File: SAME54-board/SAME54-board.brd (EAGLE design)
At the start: 70.8 x 119.4 mm, 33 parts, among them IC1 ATSAME54N20A-AUT, J1 GSD09002SEU, J2 CON-SOCJ-2155

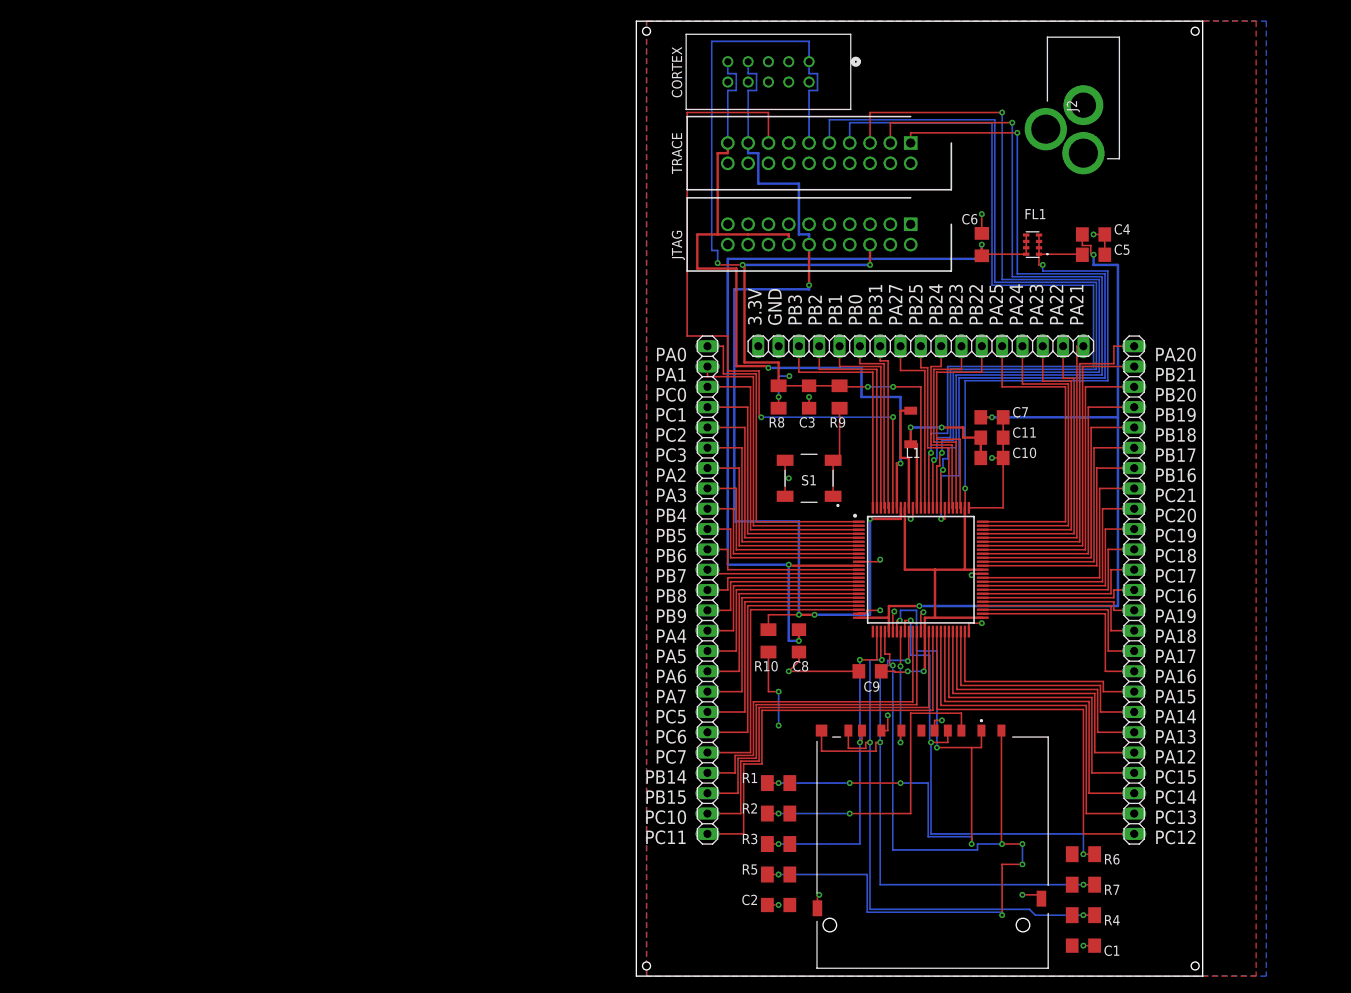
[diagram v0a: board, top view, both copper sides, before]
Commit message: Removed molex adapters and recplaed with single pin hole for each signal
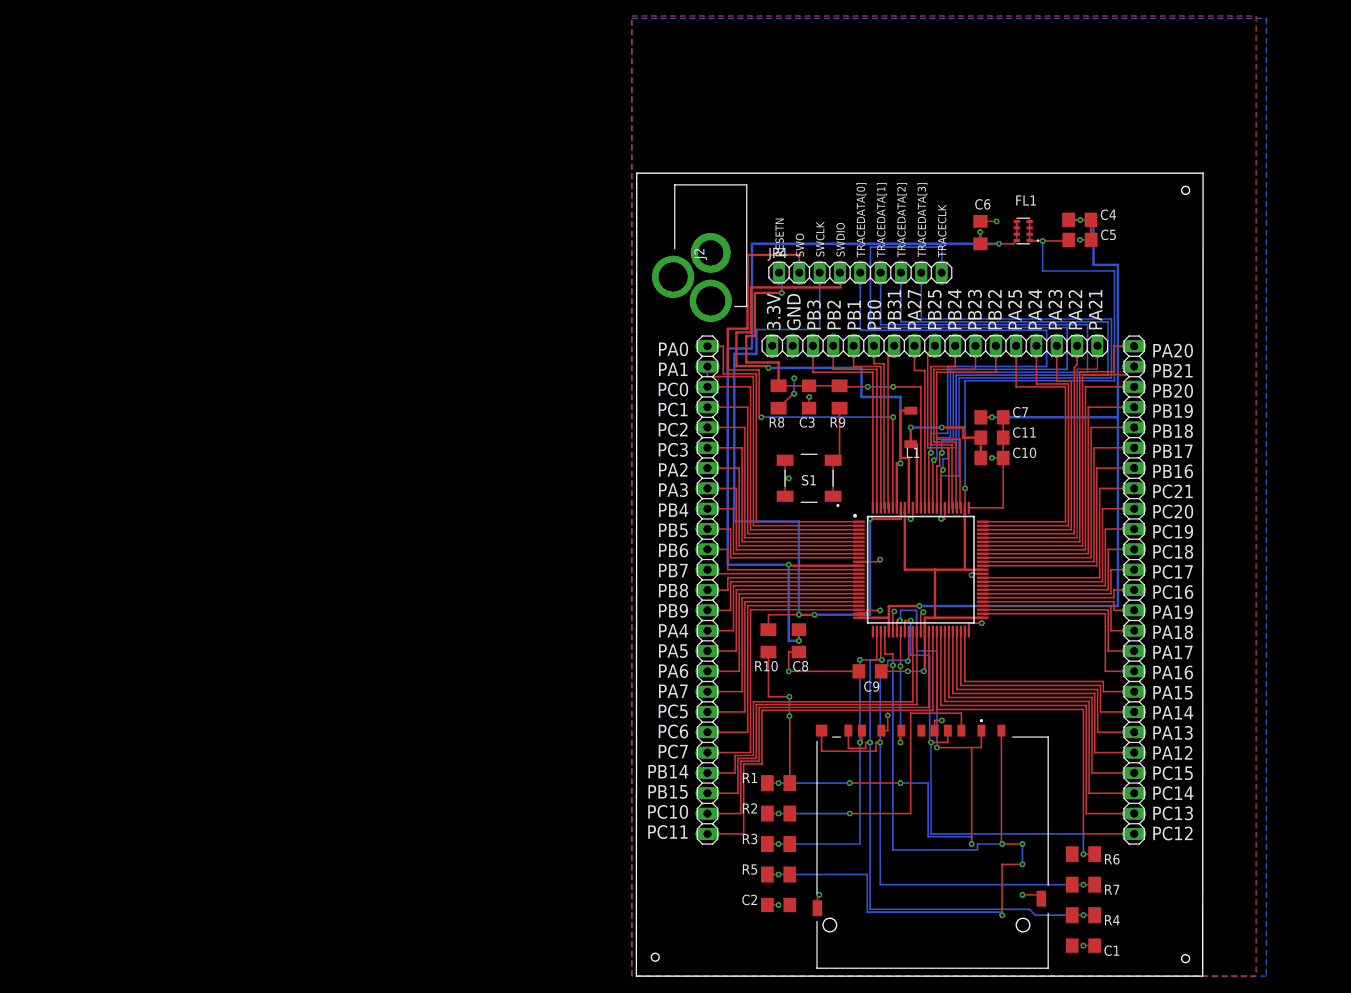
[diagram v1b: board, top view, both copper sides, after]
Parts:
- removed CORTEX: 5103308-1, SamacSys_Parts:CONN10_5103308-1
- removed JTAG, TRACE: 5103308-5, SamacSys_Parts:SHDR20W66P254_2X10_3302X914X98
- added JP4: (no value), pinhead:1X09
- moved J2 50.1 mm to (9.30, 84.4)
- moved C5 2.52 mm to (55.4, 92.0)
- moved C4 2.52 mm to (55.4, 94.5)
- moved FL1 2.06 mm to (48.4, 93.1)
- moved JP7 1.75 mm to (37.3, 78.8)
- moved C6 1.51 mm to (43.0, 92.9)
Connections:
- net GND: no longer CORTEX.6, CORTEX.8, JTAG.11, JTAG.13, JTAG.15, JTAG.17, JTAG.19, JTAG.3, JTAG.5, JTAG.7, JTAG.9, TRACE.12, TRACE.16, TRACE.18, TRACE.2, TRACE.4, TRACE.6
- net RESETN: now also JP4.1; no longer CORTEX.1, JTAG.6, TRACE.11
- net SWDCLK: now also JP4.3; no longer CORTEX.7, JTAG.12, TRACE.17
- net SWDIO: now also JP4.4; no longer CORTEX.9, JTAG.14, TRACE.19
- net SWO: now also JP4.2; no longer TRACE.15
- net TRACECLK: now also JP4.9; no longer TRACE.9
- net TRACEDATA[0]: now also JP4.5; no longer TRACE.7
- net TRACEDATA[1]: now also JP4.6; no longer TRACE.5
- net TRACEDATA[2]: now also JP4.7; no longer TRACE.3
- net TRACEDATA[3]: now also JP4.8; no longer TRACE.1
- net VCC: no longer CORTEX.10, JTAG.20, TRACE.20
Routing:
- net RESETN: track 129.9 -> 56.0 mm, vias 5 -> 3
- net SWDCLK: track 128.1 -> 93.3 mm, vias 4 -> 3
- net TRACEDATA[0]: track 101.8 -> 67.4 mm
- net SWDIO: track 97.7 -> 63.5 mm
- net TRACEDATA[1]: track 102.2 -> 74.2 mm, vias 2 -> 1
- net SWO: track 89.2 -> 63.8 mm
- net TRACEDATA[2]: track 97.3 -> 76.2 mm, vias 2 -> 1
- net TRACECLK: track 105.2 -> 86.2 mm
- net TRACEDATA[3]: track 96.1 -> 77.7 mm, vias 2 -> 1
- net VCC: track 15.8 -> 23.7 mm
- net VDDIOB: track 103.8 -> 107.4 mm
- net VDDIO: track 116.9 -> 119.1 mm
- net N$66: track 24.2 -> 26.0 mm
- net N$65: track 26.5 -> 28.3 mm
- net N$64: track 28.9 -> 30.7 mm
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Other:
- board size 70.8 x 119.4 mm -> 70.8 x 100.4 mm
- board text added: "RESETN SWO SWCLK SWDIO TRACEDATA[0] TRACEDATA[1] TRACEDATA[2] TRACEDATA[3] TRACECLK"

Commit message: New board design for better space managemnt
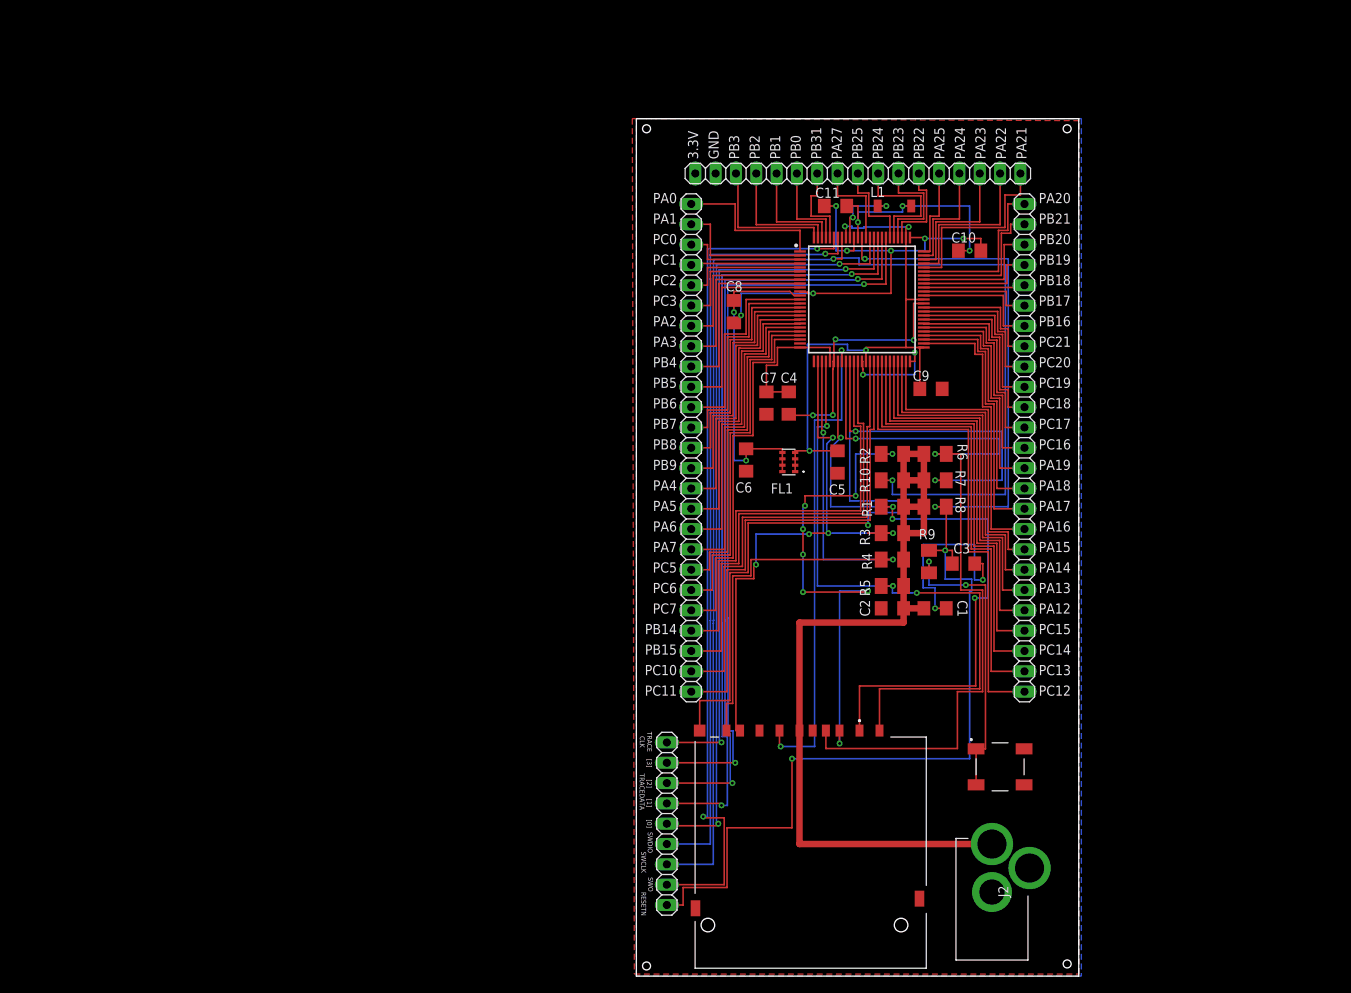
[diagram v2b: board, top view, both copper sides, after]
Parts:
- moved J2 76.5 mm to (44.5, 16.5), turned to 90 degrees
- moved JP4 73.0 mm to (3.81, 19.1), turned to 90 degrees
- moved R7 53.8 mm to (37.3, 62.0)
- moved R6 53.4 mm to (37.3, 65.3)
- moved R4 50.5 mm to (32.0, 52.1), turned to 0 degrees
- moved R2 47.2 mm to (32.0, 65.3)
- moved C1 46.1 mm to (37.3, 46.0)
- moved S1 43.3 mm to (45.5, 26.2), turned to 0 degrees
- moved C4 43.0 mm to (19.1, 71.6), turned to 270 degrees
- moved C8 41.9 mm to (12.2, 83.1)
- moved R3 41.4 mm to (32.0, 55.4)
- moved FL1 41.1 mm to (19.1, 64.3)
- moved C5 41.1 mm to (25.1, 64.3), turned to 270 degrees
- moved C6 40.8 mm to (13.7, 64.5), turned to 270 degrees
- moved C2 39.7 mm to (32.0, 46.0)
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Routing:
- net RESETN: track 56.0 -> 158.2 mm, vias 3 -> 4
- net VDDIOB: track 107.4 -> 18.0 mm, vias 3 -> 0
- net VCC: track 23.7 -> 108.4 mm, vias 4 -> 0
- net SWDCLK: track 93.3 -> 168.7 mm, vias 3 -> 2
- net VDDANA: track 111.4 -> 40.0 mm, vias 4 -> 2
- net GND: track 71.5 -> 134.6 mm, vias 19 -> 15
- net VDDIO: track 119.1 -> 71.5 mm
- net SDCD: track 57.9 -> 103.4 mm, vias 3 -> 2
- net SDCK: track 15.5 -> 60.9 mm
- net SWO: track 63.8 -> 106.9 mm
- net SDWP: track 73.2 -> 113.4 mm
- net SWDIO: track 63.5 -> 97.2 mm, vias 2 -> 1
- net TRACEDATA[0]: track 67.4 -> 99.6 mm, vias 1 -> 2
- net SDDAT[0]: track 42.0 -> 73.6 mm, vias 3 -> 5
- net N$28: track 38.5 -> 11.7 mm
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- added copper zone on layer 1, net GND
- added copper zone on layer 16, net VCC
- removed copper zone on layer 16, net GND
- removed copper zone on layer 1, net VCC
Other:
- board size 70.8 x 100.4 mm -> 55.3 x 107.2 mm
- board text added: "RESETN"
- board text added: "SWCLK"
- board text added: "SWDIO"
- board text added: "SWO"
- board text added: "TRACE CLK"
- board text added: "TRACEDATA"
- board text added: "[0]"
- board text added: "[1]"
- board text added: "[2]"
- board text added: "[3]"
- board text removed: "RESETN SWO SWCLK SWDIO TRACEDATA[0] TRACEDATA[1] TRACEDATA[2] TRACEDATA[3] TRACECLK"

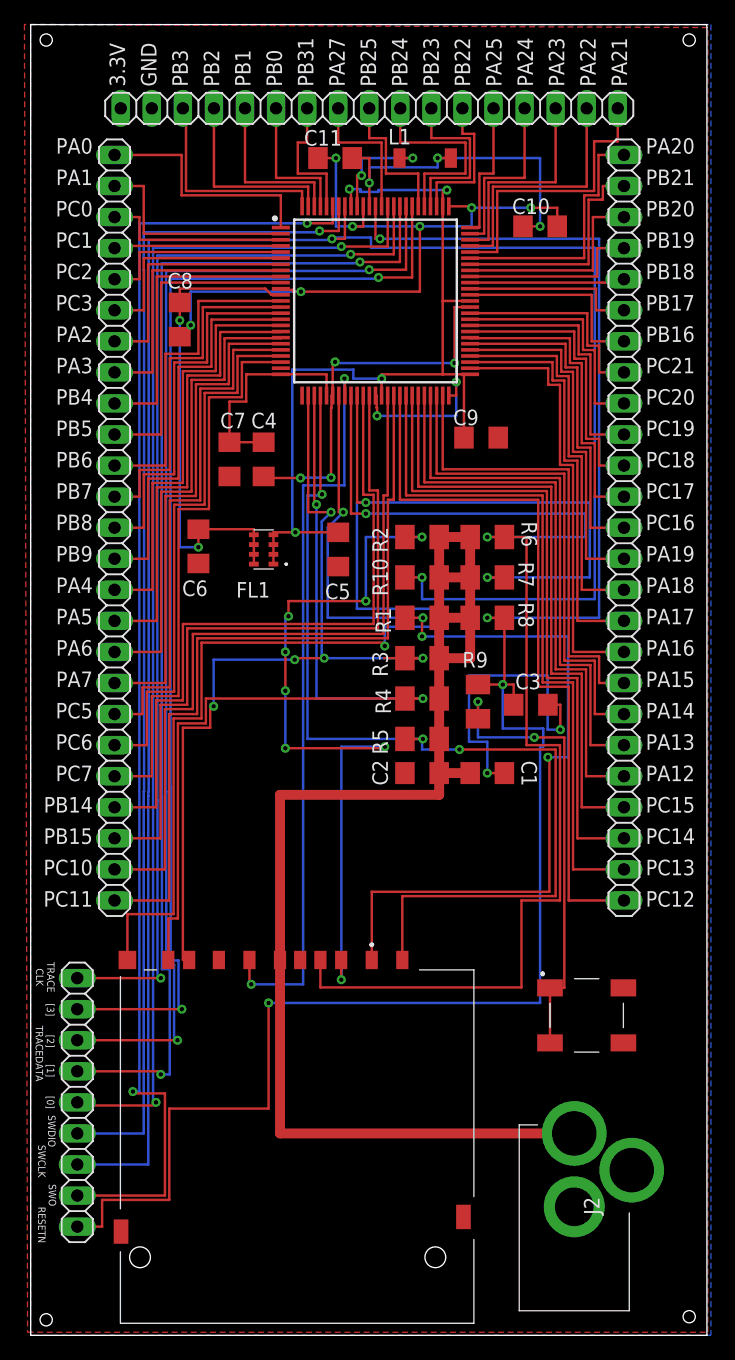
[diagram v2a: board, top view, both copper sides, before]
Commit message: Added label for Reset and increased hole dimensions to 3.2mm
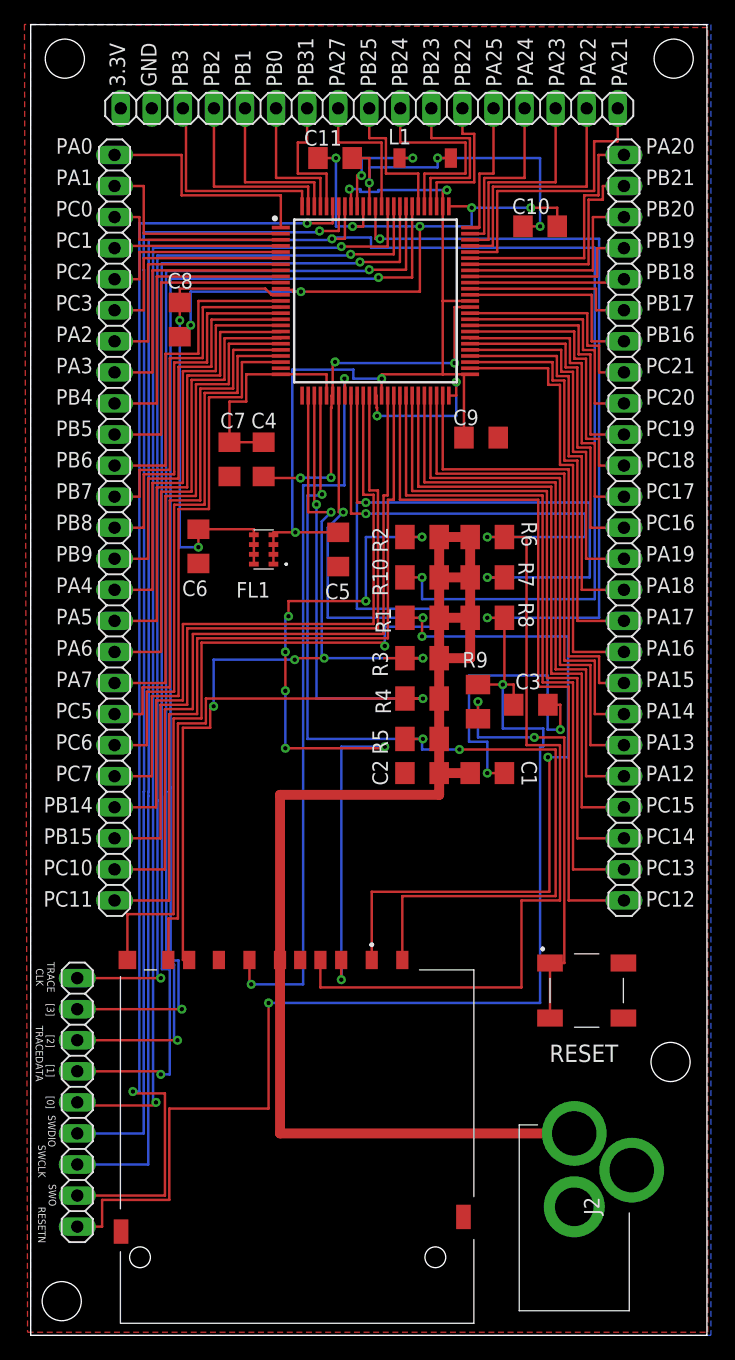
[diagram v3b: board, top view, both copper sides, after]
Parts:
- moved S1 2.03 mm to (45.5, 28.2)
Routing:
- net N$4: track 37.5 -> 35.5 mm
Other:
- board text added: "RESET"
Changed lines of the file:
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@@
 <wire x1="55.296" y1="107.178" x2="0" y2="107.178" width="0" layer="20"/>
 <wire x1="0" y1="107.178" x2="0" y2="0" width="0" layer="20"/>
-<hole x="1.27" y="1.27" drill="1"/>
-<hole x="53.848" y="1.524" drill="1"/>
-<hole x="1.27" y="105.918" drill="1"/>
-<hole x="53.848" y="105.918" drill="1"/>
 <text x="48.768" y="102.108" size="1.27" layer="21" distance="102" rot="R90">3.3V
 GND
@@
 <text x="1.9558" y="29.2862" size="0.6096" layer="21" rot="SR270" align="top-center">TRACE
 CLK</text>
+<text x="42.418" y="22.352" size="1.4224" layer="21">RESET</text>
+<hole x="2.54" y="2.794" drill="3.2"/>
+<hole x="52.324" y="22.352" drill="3.2"/>
+<hole x="52.578" y="104.394" drill="3.2"/>
+<hole x="2.794" y="104.394" drill="3.2"/>
 </plain>
 <attributes>
@@
 <attribute name="SPICEPREFIX" value="R" x="-19.304" y="-5.334" size="1.778" layer="27" rot="R270" display="off"/>
 </element>
-<element name="S1" library="SamacSys_Parts" package="LL3301BF065QJ" value="LL3301BF065QJ" x="45.466" y="26.162" smashed="yes">
-<attribute name="DESCRIPTION" value="Pushbutton Switches 50mA 12VDC F065 9.5mm J-Lead" x="84.836" y="-9.398" size="1.778" layer="27" display="off"/>
-<attribute name="HEIGHT" value="9.8mm" x="84.836" y="-9.398" size="1.778" layer="27" display="off"/>
-<attribute name="MANUFACTURER_NAME" value="E-Switch" x="84.836" y="-9.398" size="1.778" layer="27" display="off"/>
-<attribute name="MANUFACTURER_PART_NUMBER" value="LL3301BF065QJ" x="84.836" y="-9.398" size="1.778" layer="27" display="off"/>
-<attribute name="MOUSER_PART_NUMBER" value="612-LL3301BF065QJ" x="84.836" y="-9.398" size="1.778" layer="27" display="off"/>
-<attribute name="MOUSER_PRICE-STOCK" value="https://www.mouser.co.uk/ProductDetail/E-Switch/LL3301BF065QJ?qs=QtyuwXswaQgf5j8qoJZz7w%3D%3D" x="84.836" y="-9.398" size="1.778" layer="27" display="off"/>
+<element name="S1" library="SamacSys_Parts" package="LL3301BF065QJ" value="LL3301BF065QJ" x="45.466" y="28.194" smashed="yes">
+<attribute name="DESCRIPTION" value="Pushbutton Switches 50mA 12VDC F065 9.5mm J-Lead" x="84.836" y="-7.366" size="1.778" layer="27" display="off"/>
+<attribute name="HEIGHT" value="9.8mm" x="84.836" y="-7.366" size="1.778" layer="27" display="off"/>
+<attribute name="MANUFACTURER_NAME" value="E-Switch" x="84.836" y="-7.366" size="1.778" layer="27" display="off"/>
+<attribute name="MANUFACTURER_PART_NUMBER" value="LL3301BF065QJ" x="84.836" y="-7.366" size="1.778" layer="27" display="off"/>
+<attribute name="MOUSER_PART_NUMBER" value="612-LL3301BF065QJ" x="84.836" y="-7.366" size="1.778" layer="27" display="off"/>
+<attribute name="MOUSER_PRICE-STOCK" value="https://www.mouser.co.uk/ProductDetail/E-Switch/LL3301BF065QJ?qs=QtyuwXswaQgf5j8qoJZz7w%3D%3D" x="84.836" y="-7.366" size="1.778" layer="27" display="off"/>
 </element>
 </elements>
@@
 <contactref element="S1" pad="3"/>
 <contactref element="R9" pad="2"/>
-<wire x1="42.466" y1="28.412" x2="43.6372" y2="28.412" width="0.2032" layer="1"/>
+<wire x1="42.466" y1="30.444" x2="43.6372" y2="30.444" width="0.2032" layer="1"/>
 <wire x1="43.6372" y1="48.8922" x2="41.1802" y2="48.8922" width="0.2032" layer="1"/>
 <via x="41.1802" y="48.8922" extent="1-16" drill="0.35"/>
@@
 <via x="36.576" y="51.816" extent="1-16" drill="0.35"/>
 <wire x1="36.576" y1="51.816" x2="36.576" y2="50.416" width="0.2032" layer="1"/>
-<wire x1="43.6372" y1="28.412" x2="43.6372" y2="48.8922" width="0.2032" layer="1"/>
-<wire x1="42.466" y1="28.412" x2="42.466" y2="23.912" width="0.2032" layer="1"/>
+<wire x1="43.6372" y1="30.444" x2="43.6372" y2="48.8922" width="0.2032" layer="1"/>
+<wire x1="42.466" y1="30.444" x2="42.466" y2="25.944" width="0.2032" layer="1"/>
 </signal>
 </signals>
